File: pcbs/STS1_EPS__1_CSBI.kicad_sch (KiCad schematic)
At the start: 6 parts

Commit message: Worked on STS1_EPS_2.
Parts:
- CSBI_1: value CSBI_1 -> ESQT-125-02-F-D-800
- CSBI_2: value CSBI_2 -> ESQT-125-02-F-D-800
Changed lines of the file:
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@@
     (in_bom yes) (on_board yes)
     (property "Reference" "CSBI_1" (id 0) (at 93.98 38.9382 0))
-    (property "Value" "CSBI_1" (id 1) (at 93.98 41.2496 0))
+    (property "Value" "ESQT-125-02-F-D-800" (id 1) (at 93.98 41.2496 0))
     (property "Footprint" "Connector_PinHeader_2.00mm:PinHeader_2x25_P2.00mm_Vertical" (id 2) (at 92.71 74.93 0)
       (effects (font (size 1.27 1.27)) hide)
@@
     (in_bom yes) (on_board yes)
     (property "Reference" "CSBI_2" (id 0) (at 171.45 37.6682 0))
-    (property "Value" "CSBI_2" (id 1) (at 171.45 39.9796 0))
+    (property "Value" "ESQT-125-02-F-D-800" (id 1) (at 171.45 39.9796 0))
     (property "Footprint" "Connector_PinHeader_2.00mm:PinHeader_2x25_P2.00mm_Vertical" (id 2) (at 170.18 73.66 0)
       (effects (font (size 1.27 1.27)) hide)

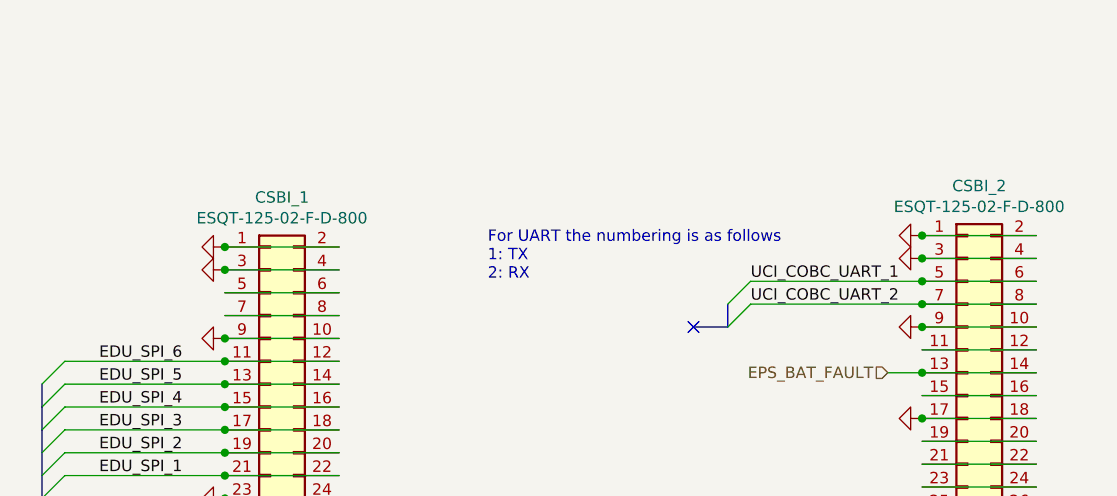
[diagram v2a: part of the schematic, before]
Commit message: Added part numbers to CSBI and inter EPS connectors. Also added some missing 3d files.
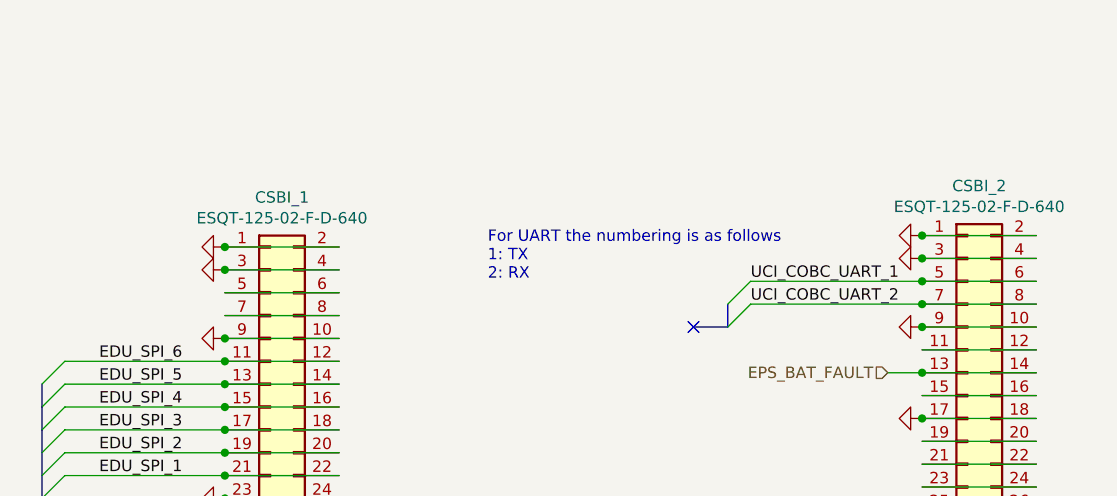
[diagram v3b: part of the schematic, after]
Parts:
- CSBI_1, CSBI_2: value ESQT-125-02-F-D-800 -> ESQT-125-02-F-D-640
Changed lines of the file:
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@@
     (in_bom yes) (on_board yes)
     (property "Reference" "CSBI_1" (id 0) (at 93.98 38.9382 0))
-    (property "Value" "ESQT-125-02-F-D-800" (id 1) (at 93.98 41.2496 0))
+    (property "Value" "ESQT-125-02-F-D-640" (id 1) (at 93.98 41.2496 0))
     (property "Footprint" "Connector_PinHeader_2.00mm:PinHeader_2x25_P2.00mm_Vertical" (id 2) (at 92.71 74.93 0)
       (effects (font (size 1.27 1.27)) hide)
@@
     (in_bom yes) (on_board yes)
     (property "Reference" "CSBI_2" (id 0) (at 171.45 37.6682 0))
-    (property "Value" "ESQT-125-02-F-D-800" (id 1) (at 171.45 39.9796 0))
+    (property "Value" "ESQT-125-02-F-D-640" (id 1) (at 171.45 39.9796 0))
     (property "Footprint" "Connector_PinHeader_2.00mm:PinHeader_2x25_P2.00mm_Vertical" (id 2) (at 170.18 73.66 0)
       (effects (font (size 1.27 1.27)) hide)

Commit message: Changed connectors of STS_EPS_1 ...again.
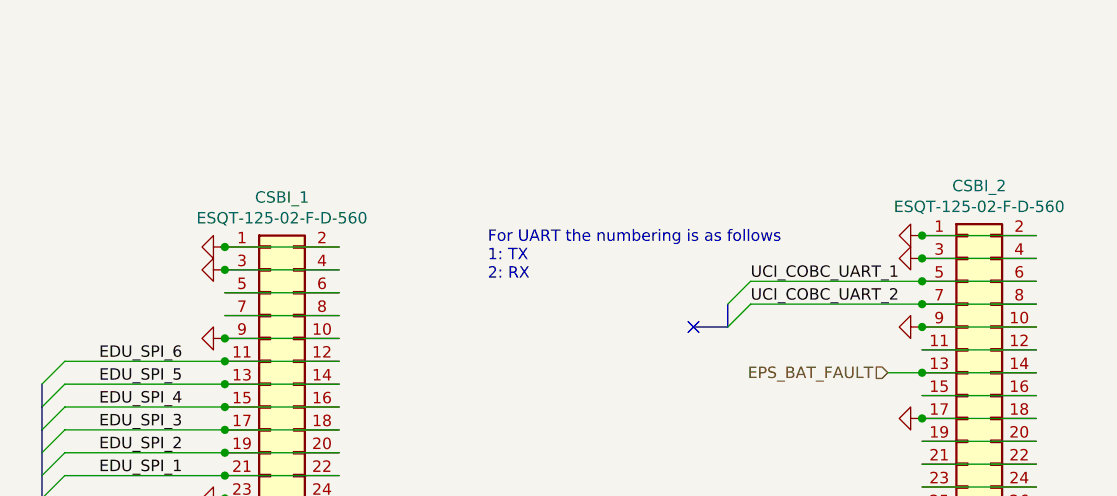
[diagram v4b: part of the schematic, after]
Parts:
- CSBI_1, CSBI_2: value ESQT-125-02-F-D-640 -> ESQT-125-02-F-D-560
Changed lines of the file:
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@@
     (in_bom yes) (on_board yes)
     (property "Reference" "CSBI_1" (id 0) (at 93.98 38.9382 0))
-    (property "Value" "ESQT-125-02-F-D-640" (id 1) (at 93.98 41.2496 0))
+    (property "Value" "ESQT-125-02-F-D-560" (id 1) (at 93.98 41.2496 0))
     (property "Footprint" "Connector_PinHeader_2.00mm:PinHeader_2x25_P2.00mm_Vertical" (id 2) (at 92.71 74.93 0)
       (effects (font (size 1.27 1.27)) hide)
@@
     (in_bom yes) (on_board yes)
     (property "Reference" "CSBI_2" (id 0) (at 171.45 37.6682 0))
-    (property "Value" "ESQT-125-02-F-D-640" (id 1) (at 171.45 39.9796 0))
+    (property "Value" "ESQT-125-02-F-D-560" (id 1) (at 171.45 39.9796 0))
     (property "Footprint" "Connector_PinHeader_2.00mm:PinHeader_2x25_P2.00mm_Vertical" (id 2) (at 170.18 73.66 0)
       (effects (font (size 1.27 1.27)) hide)

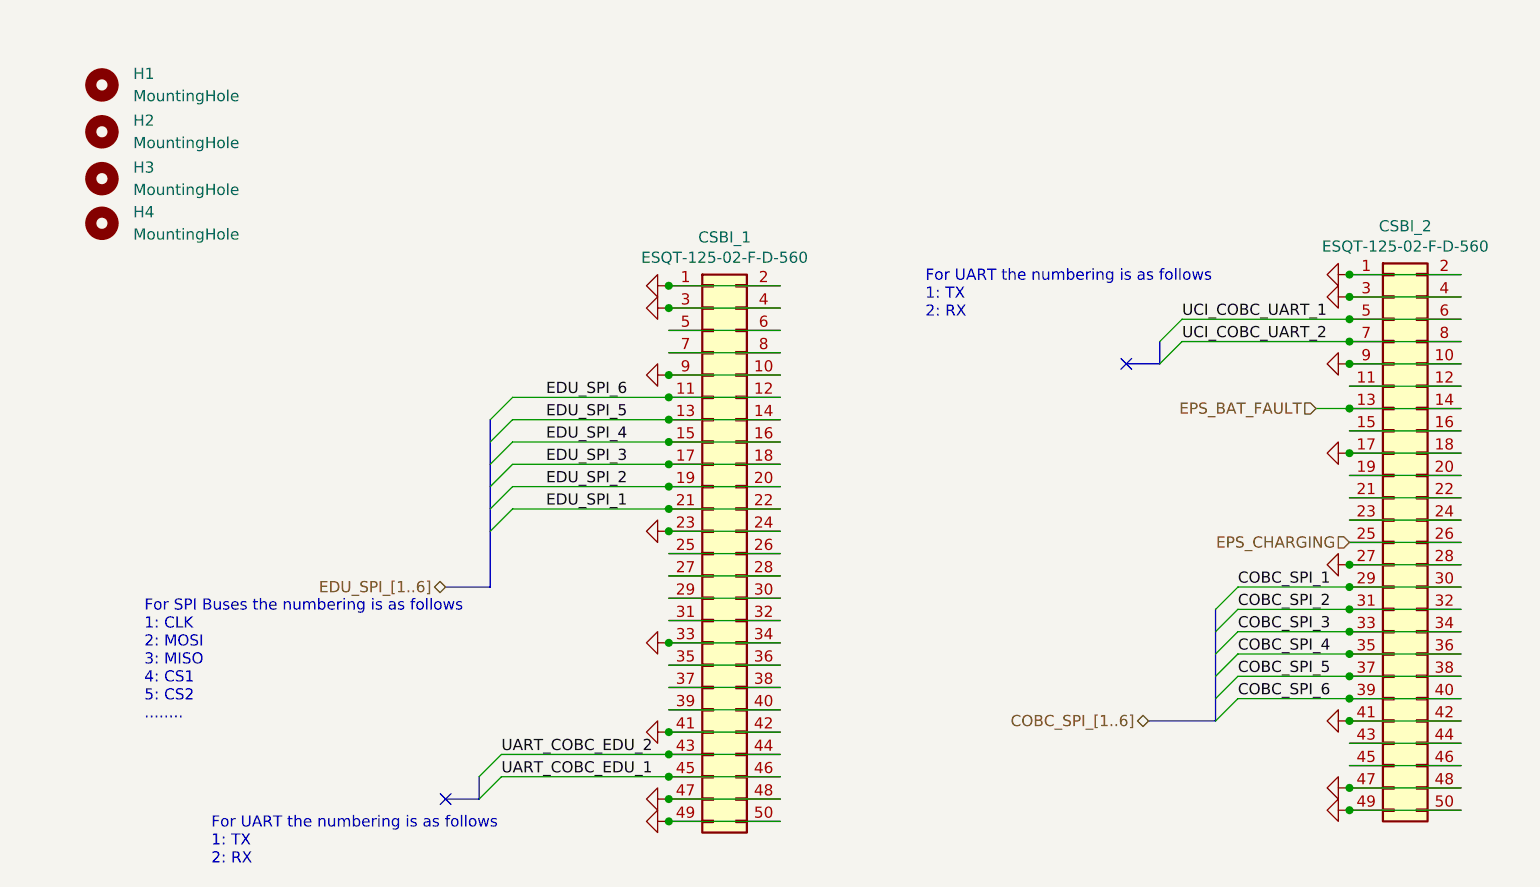
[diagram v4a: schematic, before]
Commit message: Ported kicad projects to KiCad 8.0.
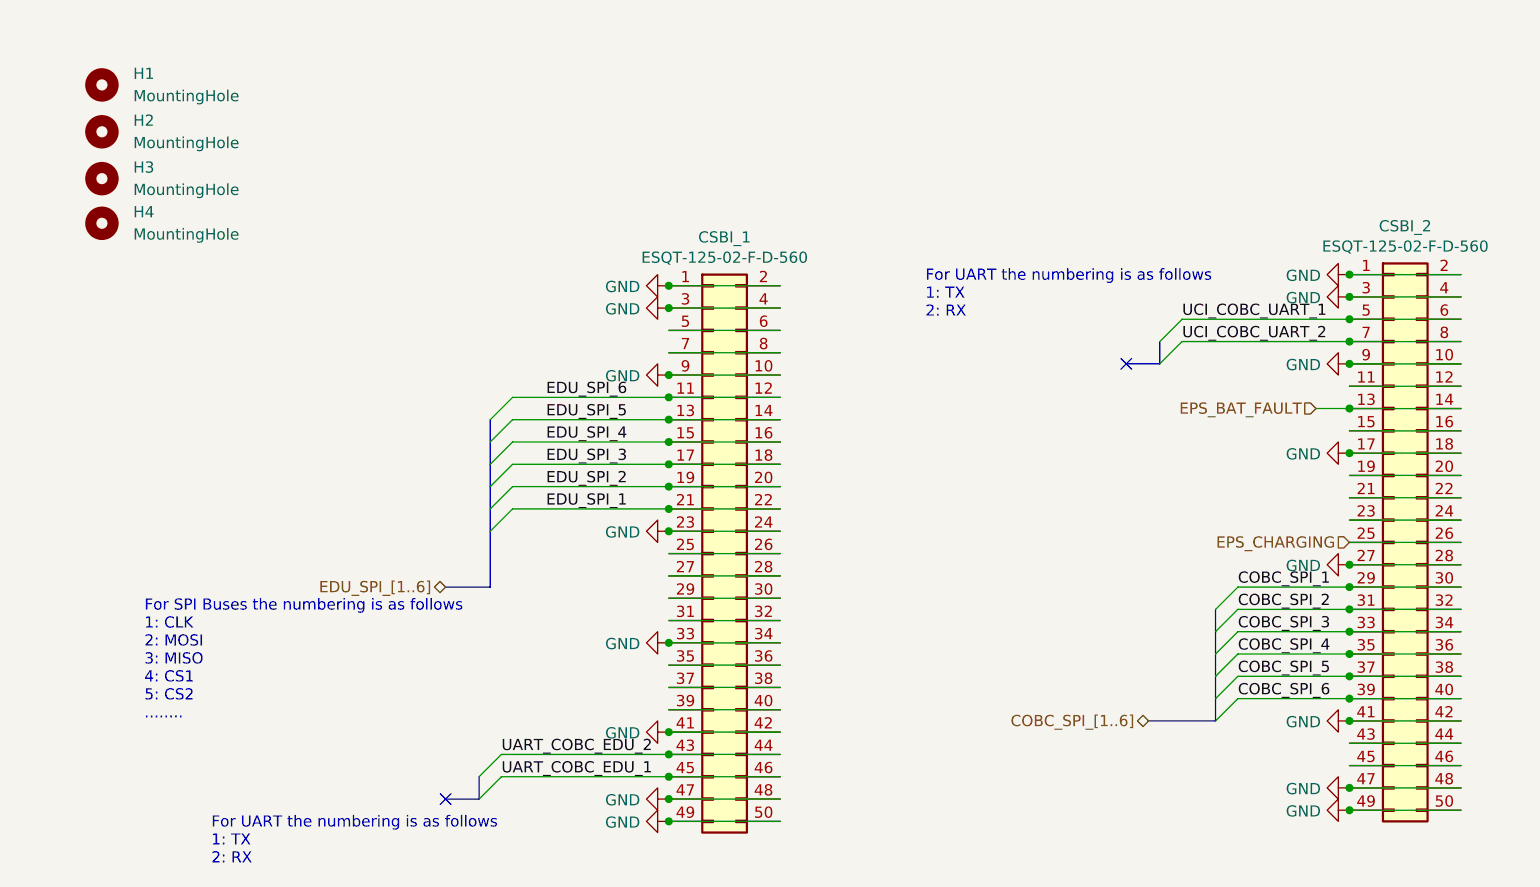
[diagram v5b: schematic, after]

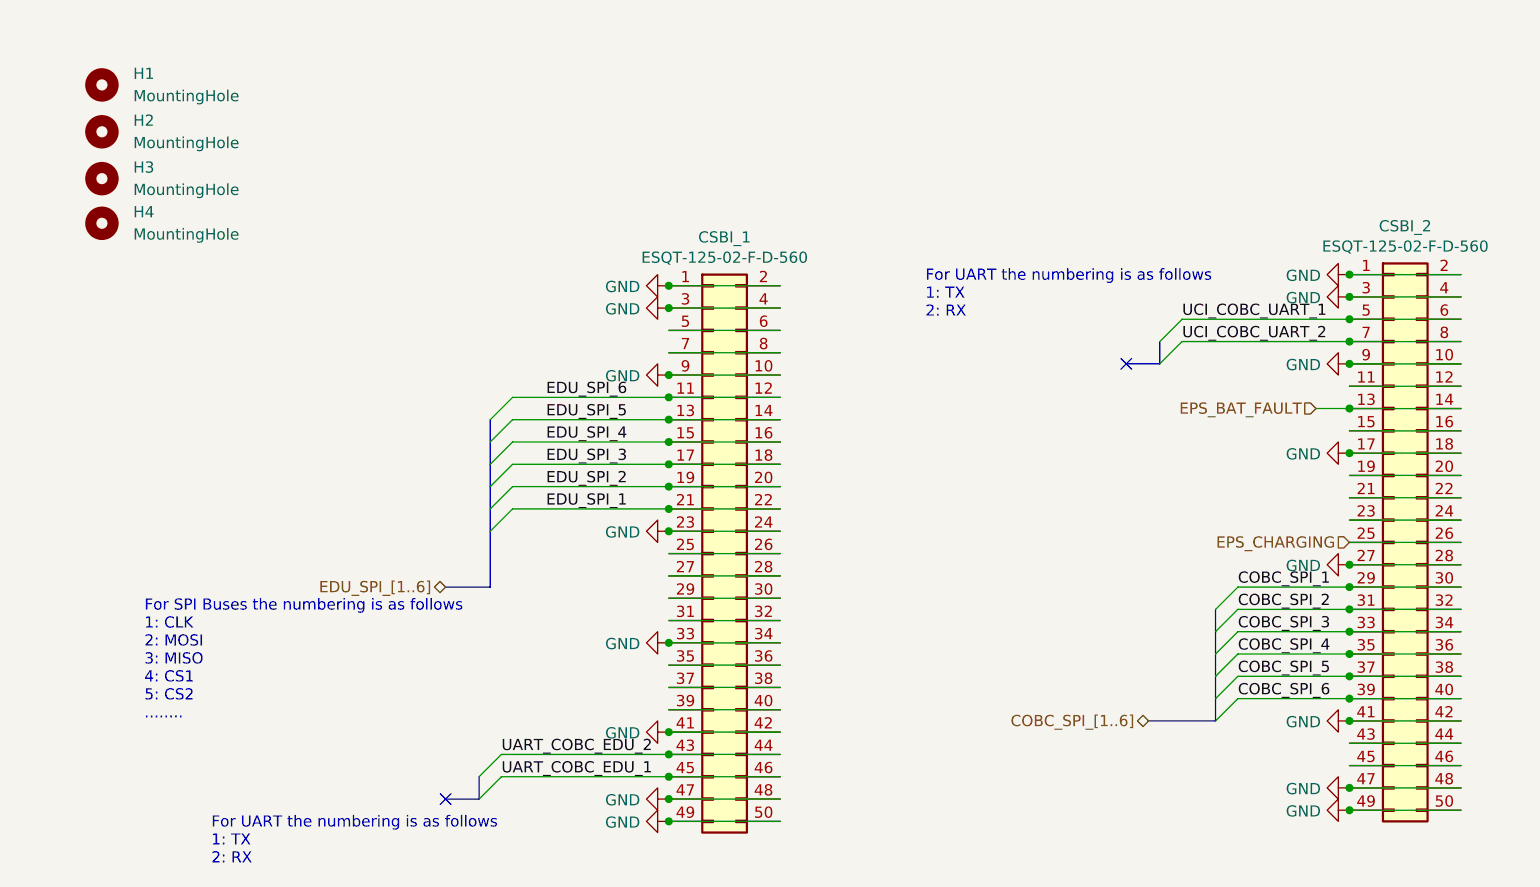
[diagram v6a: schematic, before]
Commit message: Adjusted CSBI so it conforms to the new version of it.
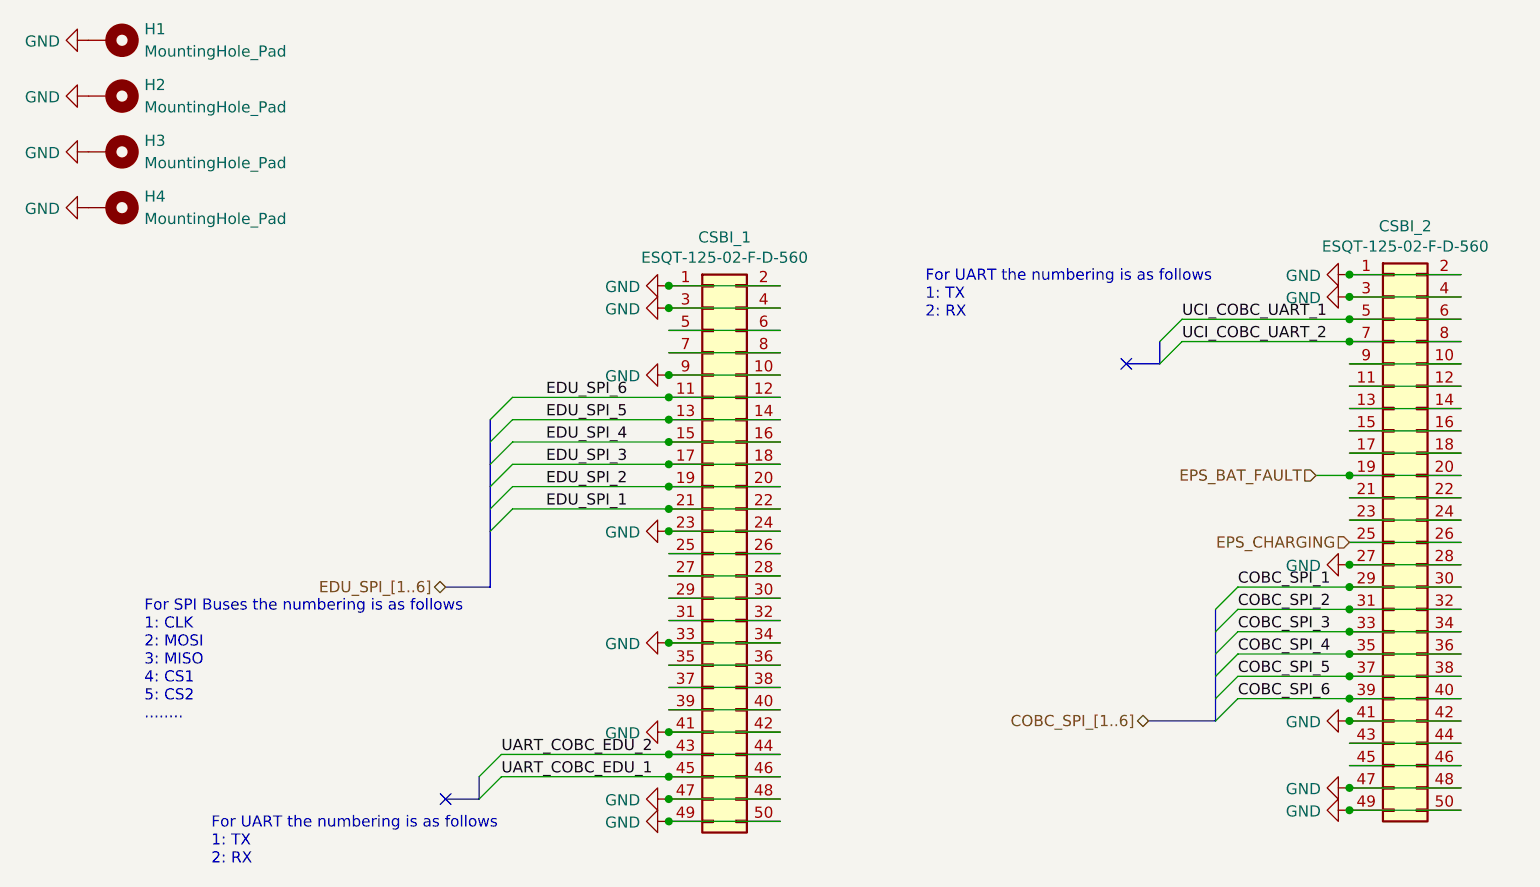
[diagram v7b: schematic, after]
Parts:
- removed H1, H2, H3, H4: MountingHole, MountingHole:MountingHole_4.3mm_M4_Pad_Via, symbol Mechanical:MountingHole
- added H1, H2, H3, H4: MountingHole_Pad, MountingHole:MountingHole_4.3mm_M4_Pad_Via, symbol Mechanical:MountingHole_Pad
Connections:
- net EPS_BAT_FAULT: now also CSBI_2.19 (Pin_19), CSBI_2.20 (Pin_20); no longer CSBI_2.13 (Pin_13), CSBI_2.14 (Pin_14)
- net GND: now also H1.1, H2.1, H3.1, H4.1; no longer CSBI_2.10 (Pin_10), CSBI_2.17 (Pin_17), CSBI_2.18 (Pin_18), CSBI_2.9 (Pin_9)
- new net: CSBI_2.10 (Pin_10), CSBI_2.9 (Pin_9)
- new net: CSBI_2.13 (Pin_13), CSBI_2.14 (Pin_14)
- new net: CSBI_2.17 (Pin_17), CSBI_2.18 (Pin_18)
